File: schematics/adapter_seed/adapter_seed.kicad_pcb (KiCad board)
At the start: 2 copper layers, 2 parts, among them J1 Conn_02x20_Odd_Even

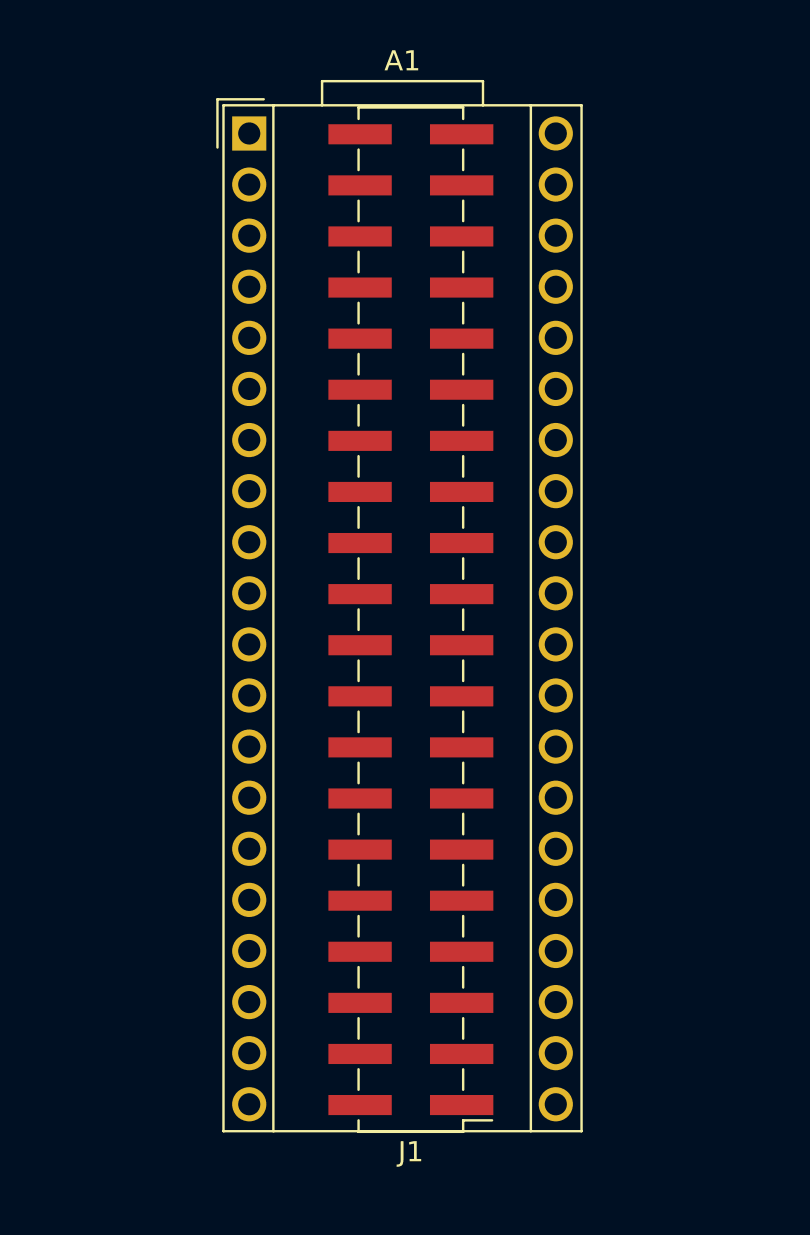
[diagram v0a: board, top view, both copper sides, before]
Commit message: daisy seed adapter board: initial layout
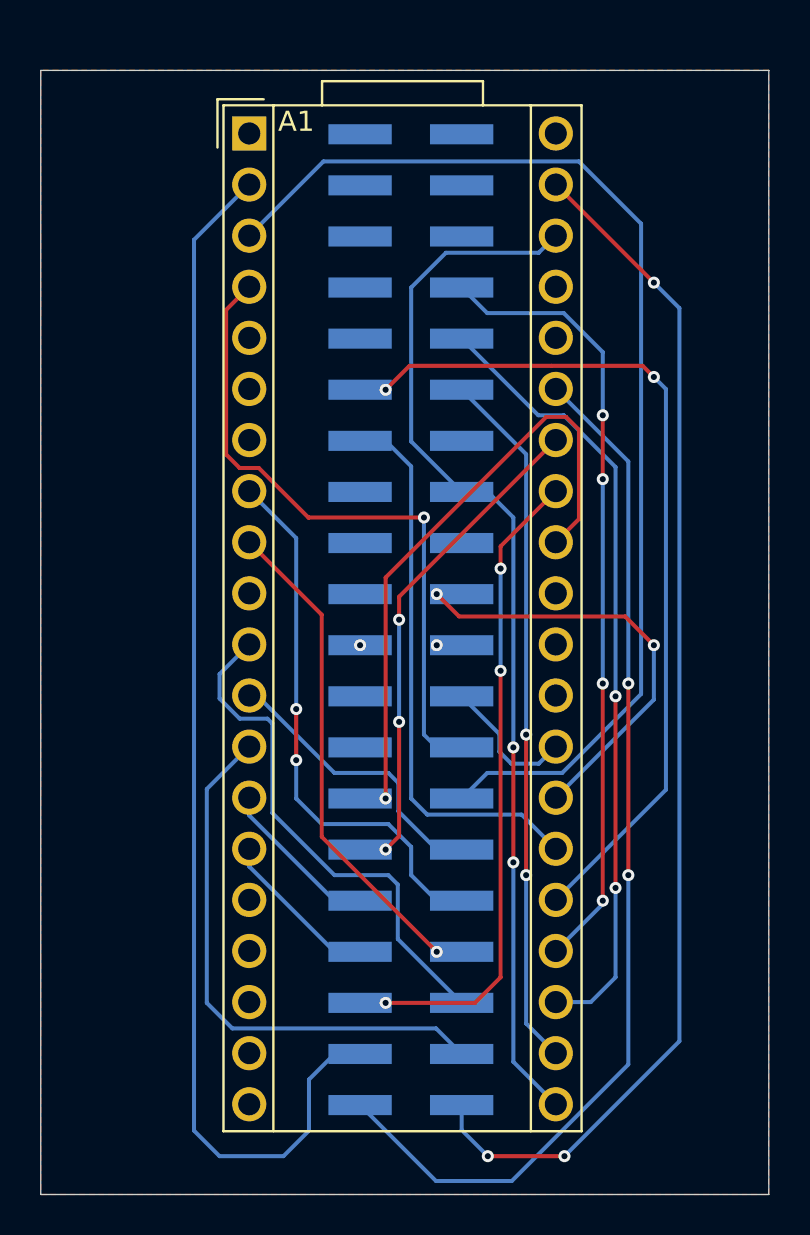
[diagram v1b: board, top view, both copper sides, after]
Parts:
- J1: moved to B.Cu
- turned J1 to 0 degrees
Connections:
- A1 pad 11: unconnected-(A1-SPI1_PICO-Pad11) -> Net-(A1-SPI1_PICO)
- A1 pad 12: unconnected-(A1-I2C1_SCL-Pad12) -> Net-(A1-I2C1_SCL)
- A1 pad 13: unconnected-(A1-I2C1_SDA-Pad13) -> Net-(A1-I2C1_SDA)
- A1 pad 14: unconnected-(A1-USART1_TX-Pad14) -> Net-(A1-USART1_TX)
- A1 pad 15: unconnected-(A1-USART1_RX-Pad15) -> Net-(A1-USART1_RX)
- A1 pad 2: unconnected-(A1-SD_DATA_3-Pad2) -> Net-(A1-SD_DATA_3)
- A1 pad 20: unconnected-(A1-AGND-Pad20) -> GND
- A1 pad 21: unconnected-(A1-3V3_A-Pad21) -> Net-(A1-3V3_A)
- A1 pad 22: unconnected-(A1-ADC_0-Pad22) -> Net-(A1-ADC_0)
- A1 pad 23: unconnected-(A1-ADC_1-Pad23) -> Net-(A1-ADC_1)
- A1 pad 24: unconnected-(A1-ADC_2-Pad24) -> Net-(A1-ADC_2)
- A1 pad 25: unconnected-(A1-ADC_3-Pad25) -> Net-(A1-ADC_3)
- A1 pad 26: unconnected-(A1-ADC_4-Pad26) -> Net-(A1-ADC_4)
- A1 pad 27: unconnected-(A1-ADC_5-Pad27) -> Net-(A1-ADC_5)
- A1 pad 28: unconnected-(A1-ADC_6-Pad28) -> Net-(A1-ADC_6)
- A1 pad 3: unconnected-(A1-SD_DATA_2-Pad3) -> Net-(A1-SD_DATA_2)
- A1 pad 32: unconnected-(A1-SAI2_SD_B-Pad32) -> Net-(A1-SAI2_SD_B)
- A1 pad 33: unconnected-(A1-SAI2_SD_A-Pad33) -> Net-(A1-SAI2_SD_A)
- A1 pad 34: unconnected-(A1-SAI2_FS-Pad34) -> Net-(A1-SAI2_FS)
- A1 pad 35: unconnected-(A1-SAI2_SCK-Pad35) -> Net-(A1-SAI2_SCK)
- A1 pad 38: unconnected-(A1-3V3_D-Pad38) -> Net-(A1-3V3_A)
- A1 pad 39: unconnected-(A1-VIN-Pad39) -> Net-(A1-VIN)
- A1 pad 4: unconnected-(A1-SD_DATA_1-Pad4) -> Net-(A1-SD_DATA_1)
- A1 pad 40: unconnected-(A1-DGND-Pad40) -> GND
- A1 pad 8: unconnected-(A1-SPI1_CS-Pad8) -> Net-(A1-SPI1_CS)
- A1 pad 9: unconnected-(A1-SPI1_SCK-Pad9) -> Net-(A1-SPI1_SCK)
- J1 pad 1: unconnected-(J1-Pin_1-Pad1) -> Net-(A1-SAI2_SCK)
- J1 pad 10: unconnected-(J1-Pin_10-Pad10) -> Net-(A1-SPI1_CS)
- J1 pad 11: unconnected-(J1-Pin_11-Pad11) -> Net-(A1-SAI2_FS)
- J1 pad 12: unconnected-(J1-Pin_12-Pad12) -> Net-(A1-I2C1_SCL)
- J1 pad 13: unconnected-(J1-Pin_13-Pad13) -> Net-(A1-SAI2_SD_B)
- J1 pad 14: unconnected-(J1-Pin_14-Pad14) -> Net-(A1-SD_DATA_2)
- J1 pad 16: unconnected-(J1-Pin_16-Pad16) -> Net-(A1-SD_DATA_1)
- J1 pad 18: unconnected-(J1-Pin_18-Pad18) -> Net-(A1-ADC_6)
- J1 pad 19: unconnected-(J1-Pin_19-Pad19) -> GND
- J1 pad 2: unconnected-(J1-Pin_2-Pad2) -> Net-(A1-VIN)
- J1 pad 20: unconnected-(J1-Pin_20-Pad20) -> GND
- J1 pad 22: unconnected-(J1-Pin_22-Pad22) -> Net-(A1-ADC_5)
- J1 pad 26: unconnected-(J1-Pin_26-Pad26) -> Net-(A1-3V3_A)
- J1 pad 27: unconnected-(J1-Pin_27-Pad27) -> Net-(A1-ADC_4)
- J1 pad 29: unconnected-(J1-Pin_29-Pad29) -> Net-(A1-ADC_3)
- J1 pad 3: unconnected-(J1-Pin_3-Pad3) -> Net-(A1-SD_DATA_3)
- J1 pad 30: unconnected-(J1-Pin_30-Pad30) -> Net-(A1-ADC_0)
- J1 pad 32: unconnected-(J1-Pin_32-Pad32) -> Net-(A1-ADC_1)
- J1 pad 34: unconnected-(J1-Pin_34-Pad34) -> Net-(A1-ADC_2)
- J1 pad 4: unconnected-(J1-Pin_4-Pad4) -> Net-(A1-I2C1_SDA)
- J1 pad 5: unconnected-(J1-Pin_5-Pad5) -> Net-(A1-SAI2_SD_A)
- J1 pad 6: unconnected-(J1-Pin_6-Pad6) -> Net-(A1-SPI1_PICO)
- J1 pad 7: unconnected-(J1-Pin_7-Pad7) -> Net-(A1-USART1_RX)
- J1 pad 8: unconnected-(J1-Pin_8-Pad8) -> Net-(A1-SPI1_SCK)
- J1 pad 9: unconnected-(J1-Pin_9-Pad9) -> Net-(A1-USART1_TX)
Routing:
- net Net-(A1-SD_DATA_3): track 0.00 -> 60.5 mm
- net Net-(A1-VIN): track 0.00 -> 60.1 mm, vias 0 -> 3
- net Net-(A1-SD_DATA_2): track 0.00 -> 56.7 mm
- net Net-(A1-3V3_A): track 0.00 -> 52.6 mm, vias 0 -> 2
- net Net-(A1-SAI2_SCK): track 0.00 -> 52.4 mm, vias 0 -> 2
- net Net-(A1-ADC_3): track 0.00 -> 42.6 mm, vias 0 -> 2
- net Net-(A1-ADC_1): track 0.00 -> 39.1 mm, vias 0 -> 2
- net Net-(A1-ADC_2): track 0.00 -> 39.1 mm, vias 0 -> 4
- net Net-(A1-ADC_0): track 0.00 -> 34.9 mm, vias 0 -> 2
- net Net-(A1-SD_DATA_1): track 0.00 -> 32.9 mm, vias 0 -> 1
- net Net-(A1-SAI2_SD_A): track 0.00 -> 31.5 mm, vias 0 -> 3
- net Net-(A1-SAI2_SD_B): track 0.00 -> 30.2 mm, vias 0 -> 1
- net Net-(A1-ADC_4): track 0.00 -> 27.8 mm
- net Net-(A1-SPI1_CS): track 0.00 -> 27.4 mm, vias 0 -> 2
- net Net-(A1-I2C1_SDA): track 0.00 -> 27.3 mm
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- added copper zone on F.Cu, net GND
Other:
- board outline added: 36.2 x 55.9 mm

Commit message: pcb: minor corrections
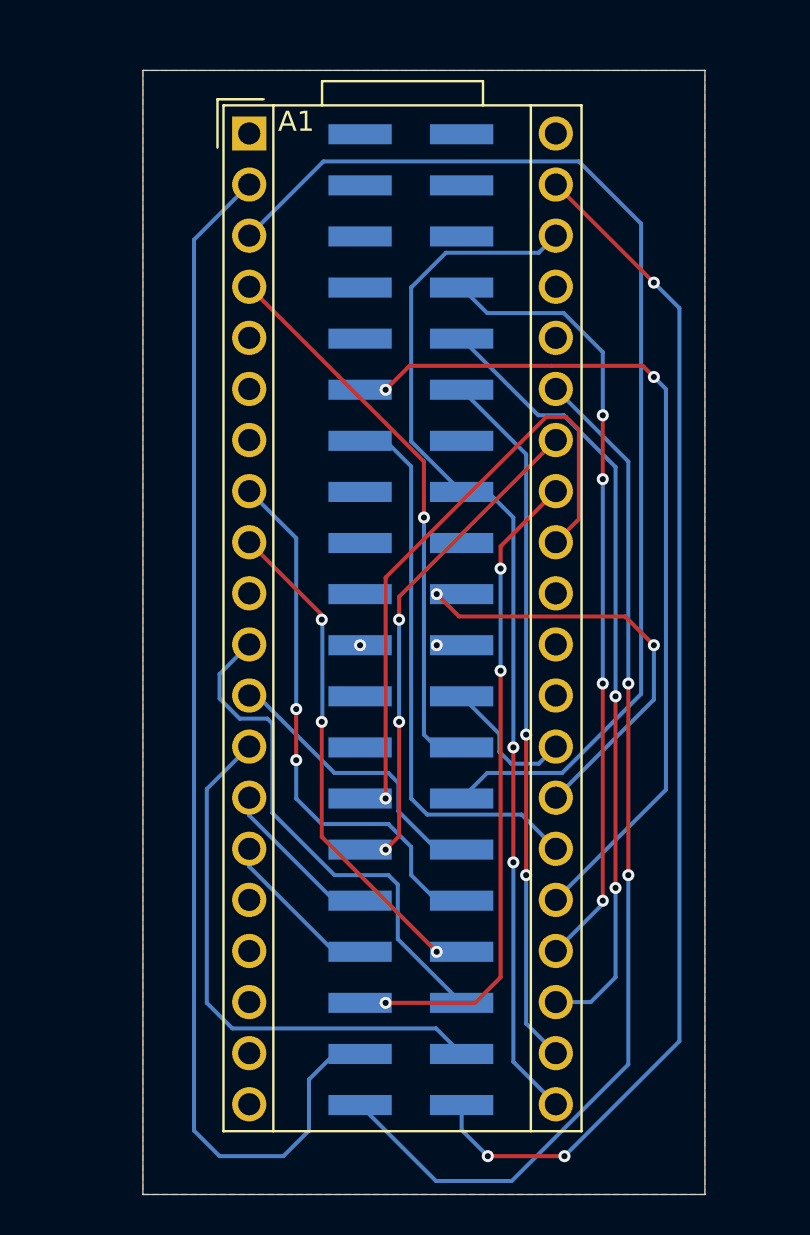
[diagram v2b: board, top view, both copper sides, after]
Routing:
- net Net-(A1-SD_DATA_1): track 32.9 -> 28.0 mm
- net Net-(A1-SPI1_SCK): track 24.2 -> 24.3 mm, vias 1 -> 3
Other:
- board size 36.2 x 55.9 mm -> 27.9 x 55.9 mm
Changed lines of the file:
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@@
     )
   )
-  (gr_rect (start 144.78 66.04) (end 180.975 121.92)
+  (gr_rect (start 149.86 66.04) (end 177.8 121.92)
     (stroke (width 0.05) (type default)) (fill none) (layer "Edge.Cuts"))
   (segment (start 158.115 116.205) (end 159.385 114.935) (width 0.2) (layer "B.Cu") (net 2))
@@
   (segment (start 166.975 100.965) (end 165.705 102.235) (width 0.2) (layer "B.Cu") (net 3))
   (segment (start 155.145 74.255) (end 158.835 70.565) (width 0.2) (layer "B.Cu") (net 3))
-  (segment (start 163.83 88.265) (end 158.115 88.265) (width 0.2) (layer "F.Cu") (net 4))
-  (segment (start 155.145 76.795) (end 153.995 77.945) (width 0.2) (layer "F.Cu") (net 4))
-  (segment (start 158.115 88.265) (end 158.098173 88.281827) (width 0.2) (layer "F.Cu") (net 4))
-  (segment (start 153.995 85.131346) (end 154.668654 85.805) (width 0.2) (layer "F.Cu") (net 4))
-  (segment (start 154.668654 85.805) (end 155.621346 85.805) (width 0.2) (layer "F.Cu") (net 4))
-  (segment (start 153.995 77.945) (end 153.995 85.131346) (width 0.2) (layer "F.Cu") (net 4))
-  (segment (start 155.621346 85.805) (end 158.098173 88.281827) (width 0.2) (layer "F.Cu") (net 4))
+  (segment (start 163.83 85.48) (end 163.83 88.265) (width 0.2) (layer "F.Cu") (net 4))
+  (segment (start 155.145 76.795) (end 163.83 85.48) (width 0.2) (layer "F.Cu") (net 4))
   (via (at 163.83 88.265) (size 0.6) (drill 0.3) (layers "F.Cu" "B.Cu") (net 4))
   (segment (start 163.83 99.06) (end 163.83 88.265) (width 0.2) (layer "B.Cu") (net 4))
@@
   (segment (start 158.75 103.505) (end 157.48 102.235) (width 0.2) (layer "B.Cu") (net 8))
   (segment (start 163.195 106.045) (end 163.195 104.64) (width 0.2) (layer "B.Cu") (net 8))
-  (segment (start 158.75 104.14) (end 158.75 93.1) (width 0.2) (layer "F.Cu") (net 9))
+  (segment (start 158.75 104.14) (end 158.75 98.425) (width 0.2) (layer "F.Cu") (net 9))
   (segment (start 158.75 93.1) (end 155.145 89.495) (width 0.2) (layer "F.Cu") (net 9))
+  (segment (start 158.75 93.345) (end 158.75 93.1) (width 0.2) (layer "F.Cu") (net 9))
   (segment (start 164.465 109.855) (end 158.75 104.14) (width 0.2) (layer "F.Cu") (net 9))
+  (via (at 158.75 98.425) (size 0.6) (drill 0.3) (layers "F.Cu" "B.Cu") (net 9))
+  (via (at 158.75 93.345) (size 0.6) (drill 0.3) (layers "F.Cu" "B.Cu") (net 9))
   (via (at 164.465 109.855) (size 0.6) (drill 0.3) (layers "F.Cu" "B.Cu") (net 9))
+  (segment (start 158.78 93.315) (end 158.75 93.345) (width 0.2) (layer "B.Cu") (net 9))
+  (segment (start 158.75 98.425) (end 158.78 98.395) (width 0.2) (layer "B.Cu") (net 9))
+  (segment (start 158.78 98.395) (end 158.78 93.315) (width 0.2) (layer "B.Cu") (net 9))
   (segment (start 156.295 102.955) (end 156.295 98.51) (width 0.2) (layer "B.Cu") (net 11))
   (segment (start 156.295 98.51) (end 156.05 98.265) (width 0.2) (layer "B.Cu") (net 11))
@@
     (polygon
       (pts
-        (xy 144.78 66.04)
-        (xy 144.78 121.92)
-        (xy 180.975 121.92)
-        (xy 180.975 66.04)
+        (xy 149.86 66.04)
+        (xy 149.86 121.92)
+        (xy 177.8 121.92)
+        (xy 177.8 66.04)
       )
     )

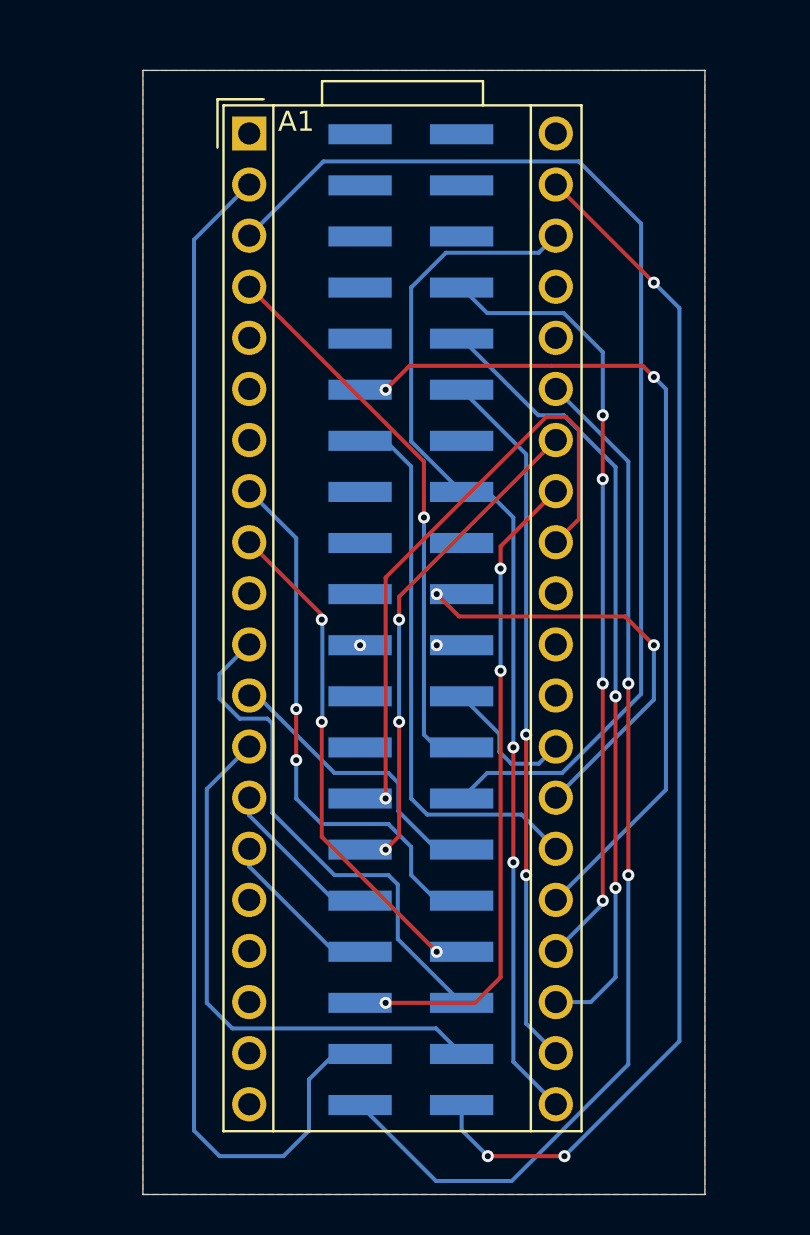
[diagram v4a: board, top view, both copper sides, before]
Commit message: avr flasher: schematic changes
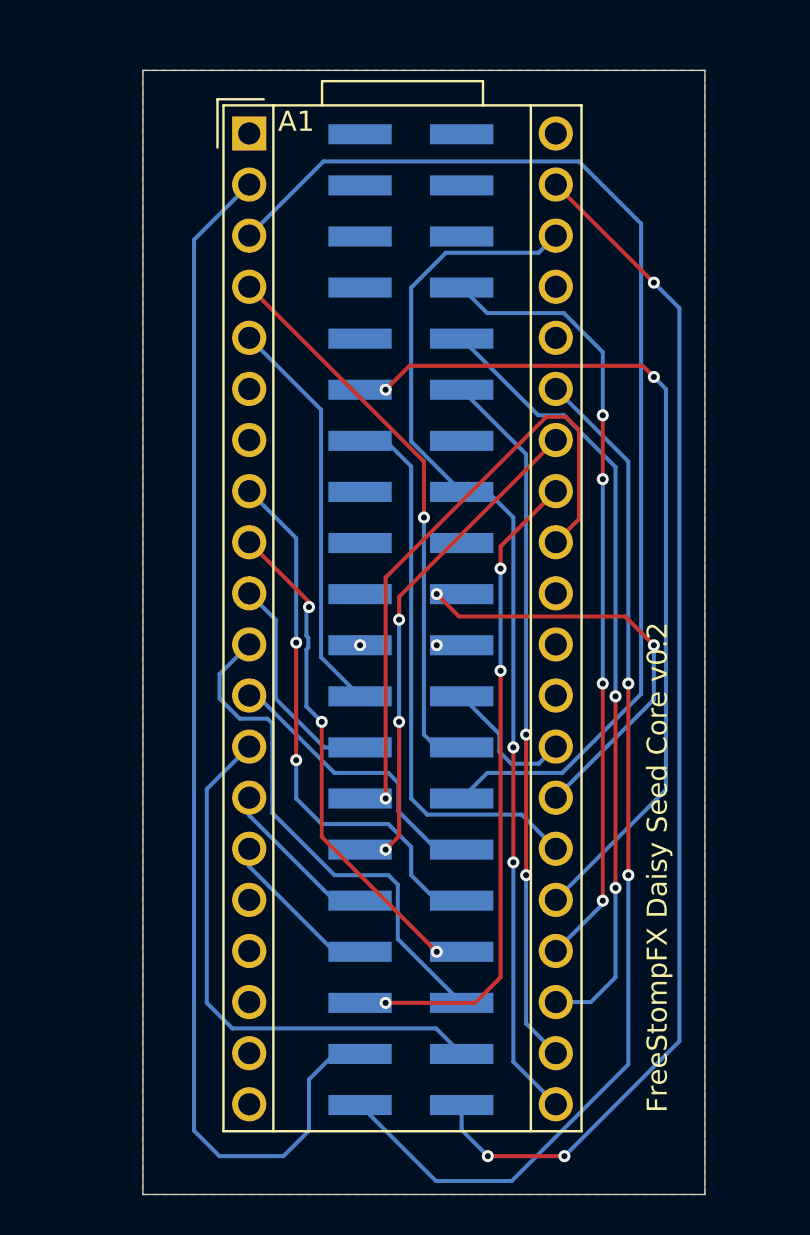
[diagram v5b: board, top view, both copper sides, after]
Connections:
- A1 pad 10: unconnected-(A1-SPI1_POCI-Pad10) -> Net-(A1-SPI1_POCI)
- A1 pad 5: unconnected-(A1-SD_DATA_0-Pad5) -> Net-(A1-SD_DATA_0)
- J1 pad 15: unconnected-(J1-Pin_15-Pad15) -> Net-(A1-SPI1_POCI)
- J1 pad 17: unconnected-(J1-Pin_17-Pad17) -> Net-(A1-SD_DATA_0)
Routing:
- net Net-(A1-SD_DATA_0): track 0.00 -> 20.1 mm
- net Net-(A1-SPI1_POCI): track 0.00 -> 11.0 mm
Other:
- board text added: "FreeStompFX Daisy Seed Core v0.2"
